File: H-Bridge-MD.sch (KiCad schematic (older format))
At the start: 67 parts, among them IC1 SI8650AB-B-IS1, IC2 A3921KLPTR-T, IC3 SI8650AB-B-IS1, IC4 A3921KLPTR-T, J1 Conn_01x02, J2 Conn_01x03, J3 Conn_01x05, J4 Conn_01x02, J5 Bus_mechaken_PCIexpress_x16_1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, Q1 NVMFD5C446NT1G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

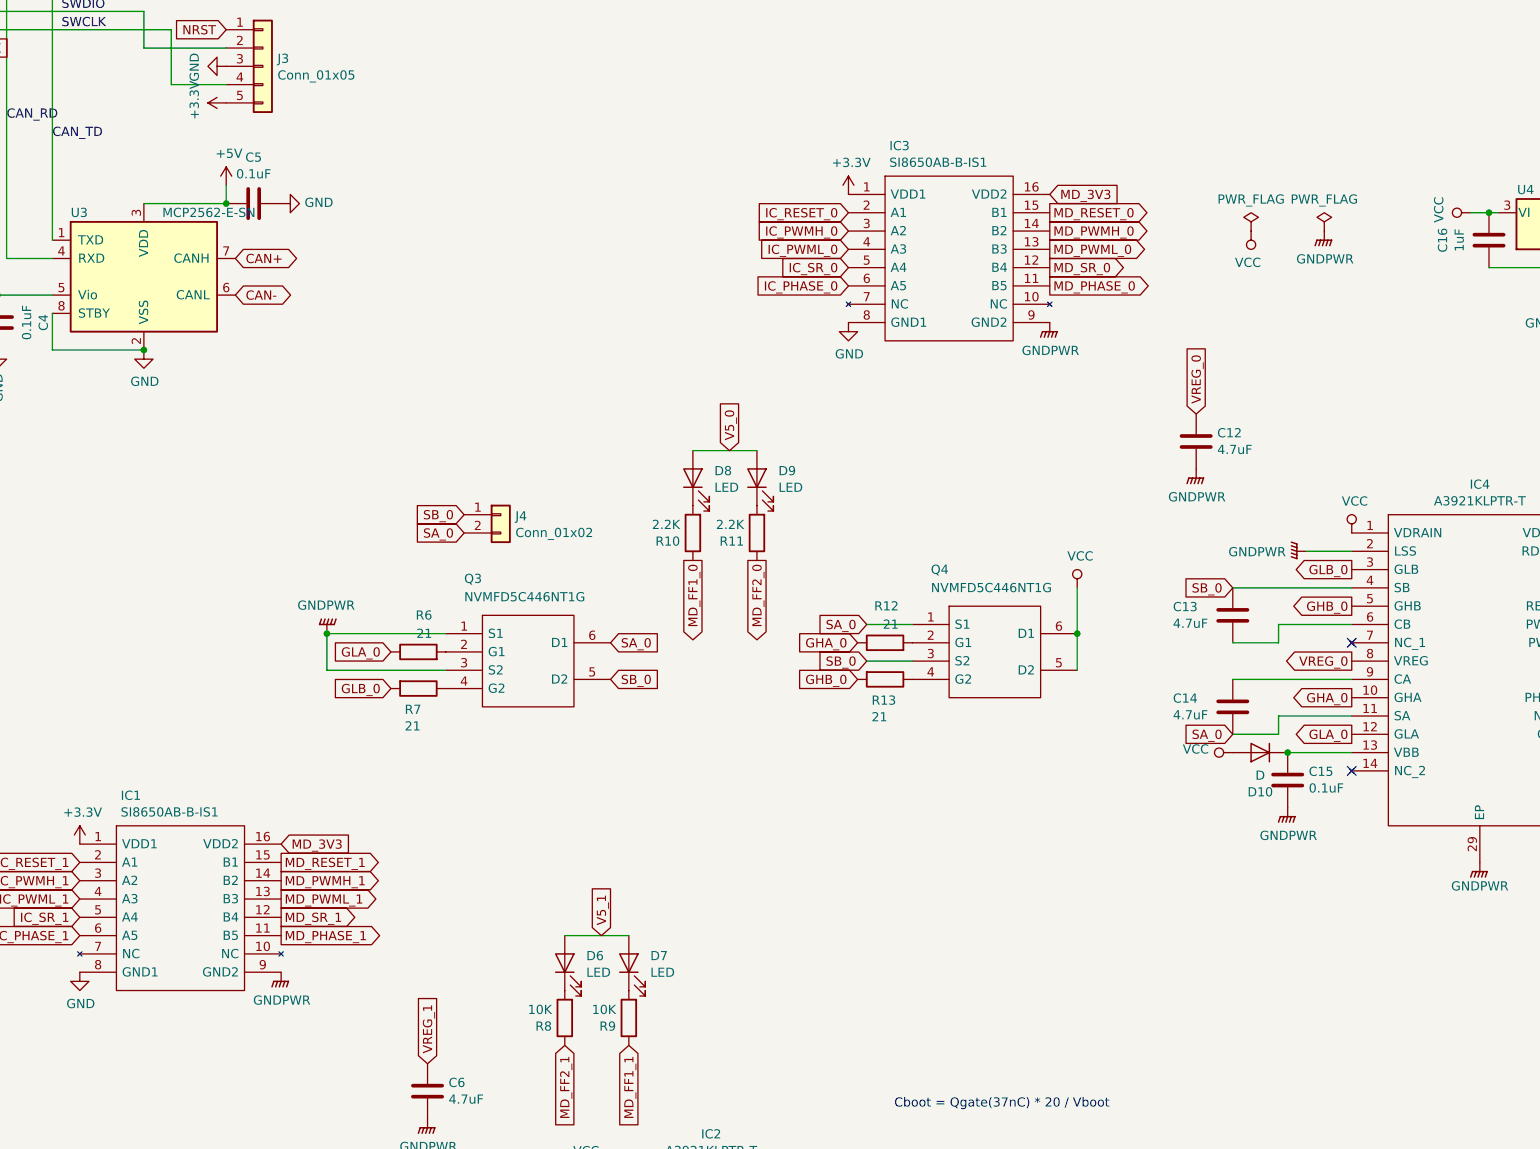
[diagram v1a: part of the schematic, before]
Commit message: change
書き込み用のピンをコンスルー対応に変更
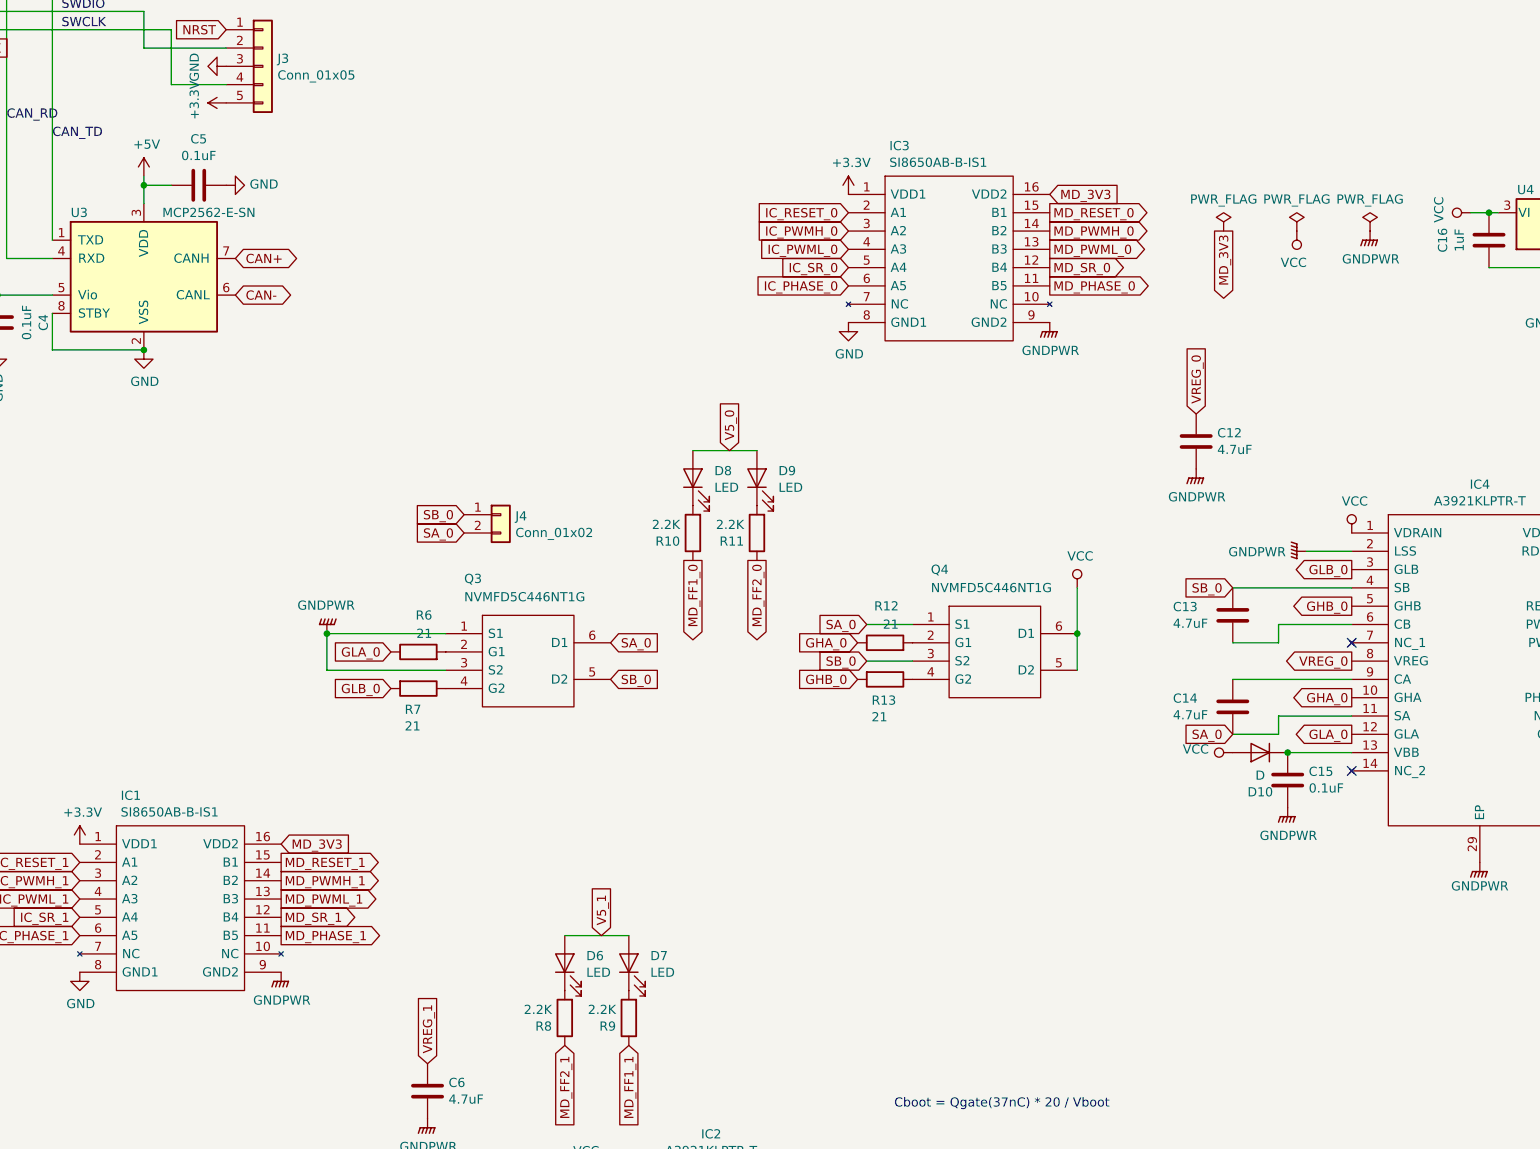
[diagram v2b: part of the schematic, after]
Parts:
- R8, R9: value 10K -> 2.2K
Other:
- moved on the sheet: C5
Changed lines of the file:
@@
-	1    0    0    -1
-$EndComp
-$Comp
-L power:PWR_FLAG #FLG04
-U 1 1 5DC02409
-P 11350 4100
-F 0 "#FLG04" H 11350 4175 50  0001 C CNN
-F 1 "PWR_FLAG" H 11350 4273 50  0000 C CNN
-F 2 "" H 11350 4100 50  0001 C CNN
-F 3 "~" H 11350 4100 50  0001 C CNN
-	1    11350 4100
-	1    0    0    -1
-$EndComp
-$Comp
-L power:PWR_FLAG #FLG05
-U 1 1 5DC02403
-P 11750 4100
-F 0 "#FLG05" H 11750 4175 50  0001 C CNN
-F 1 "PWR_FLAG" H 11750 4273 50  0000 C CNN
-F 2 "" H 11750 4100 50  0001 C CNN
-F 3 "~" H 11750 4100 50  0001 C CNN
-	1    11750 4100
 	1    0    0    -1
 $EndComp
@@
 L power:+5V #PWR022
 U 1 1 5D602945
-P 5750 3850
-F 0 "#PWR022" H 5750 3700 50  0001 C CNN
-F 1 "+5V" H 5765 4023 50  0000 C CNN
-F 2 "" H 5750 3850 50  0001 C CNN
-F 3 "" H 5750 3850 50  0001 C CNN
-	1    5750 3850
-	1    0    0    -1
-$EndComp
-Wire Wire Line
-	5750 3850 5750 3950
-Wire Wire Line
-	5750 3950 5300 3950
-$Comp
-L Device:C C5
-U 1 1 5D5F66CE
-P 5900 3950
-F 0 "C5" V 5648 3950 50  0000 C CNN
-F 1 "0.1uF" V 5739 3950 50  0000 C CNN
-F 2 "Capacitor_SMD:C_0805_2012Metric" H 5938 3800 50  0001 C CNN
-F 3 "~" H 5900 3950 50  0001 C CNN
-	1    5900 3950
-	0    1    1    0
-$EndComp
-$Comp
-L power:GND #PWR023
-U 1 1 5D5F66D4
-P 6050 3950
-F 0 "#PWR023" H 6050 3700 50  0001 C CNN
-F 1 "GND" V 6055 3822 50  0000 R CNN
-F 2 "" H 6050 3950 50  0001 C CNN
-F 3 "" H 6050 3950 50  0001 C CNN
-	1    6050 3950
-	0    -1   -1   0
-$EndComp
-Connection ~ 5750 3950
+P 5300 3800
+F 0 "#PWR022" H 5300 3650 50  0001 C CNN
+F 1 "+5V" H 5315 3973 50  0000 C CNN
+F 2 "" H 5300 3800 50  0001 C CNN
+F 3 "" H 5300 3800 50  0001 C CNN
+	1    5300 3800
+	1    0    0    -1
+$EndComp
 $Comp
 L Device:C C4
@@
 Wire Wire Line
 	9100 10800 9350 10800
-$Comp
-L power:VCC #PWR048
-U 1 1 5DC023F7
-P 11350 4100
-F 0 "#PWR048" H 11350 3950 50  0001 C CNN
-F 1 "VCC" H 11367 4273 50  0000 C CNN
-F 2 "" H 11350 4100 50  0001 C CNN
-F 3 "" H 11350 4100 50  0001 C CNN
-	1    11350 4100
-	-1   0    0    1
-$EndComp
-$Comp
-L power:GNDPWR #PWR051
-U 1 1 5DC023FD
-P 11750 4100
-F 0 "#PWR051" H 11750 3900 50  0001 C CNN
-F 1 "GNDPWR" H 11754 3946 50  0000 C CNN
-F 2 "" H 11750 4050 50  0001 C CNN
-F 3 "" H 11750 4050 50  0001 C CNN
-	1    11750 4100
-	1    0    0    -1
-$EndComp
 Connection ~ 9850 10400
 Wire Wire Line
@@
 Text GLabel 10250 4100 2    50   Output ~ 0
 MD_PWMH_0
-Text GLabel 10250 4400 2    50   Output ~ 0
-MD_PHASE_0
 Text GLabel 4200 2300 2    50   Output ~ 0
 IC_PWMH_1
-Text GLabel 10250 4000 2    50   Output ~ 0
-MD_RESET_0
 Text GLabel 3200 2400 0    50   Output ~ 0
 IC_RESET_1
@@
 	1    0    0    -1
 $EndComp
-Text GLabel 11050 5100 1    50   Input ~ 0
-VREG_0
 $Comp
 L power:GNDPWR #PWR043
@@
 P 7600 8400
 F 0 "R8" H 7670 8446 50  0000 L CNN
-F 1 "10K" H 7670 8355 50  0000 L CNN
+F 1 "2.2K" H 7670 8355 50  0000 L CNN
 F 2 "Resistor_SMD:R_0603_1608Metric" V 7530 8400 50  0001 C CNN
 F 3 "~" H 7600 8400 50  0001 C CNN
@@
 P 7950 8400
 F 0 "R9" H 8020 8446 50  0000 L CNN
-F 1 "10K" H 8020 8355 50  0000 L CNN
+F 1 "2.2K" H 8020 8355 50  0000 L CNN
 F 2 "Resistor_SMD:R_0603_1608Metric" V 7880 8400 50  0001 C CNN
 F 3 "~" H 7950 8400 50  0001 C CNN
@@
 Wire Wire Line
 	7600 7950 7950 7950
+Text GLabel 10250 4000 2    50   Output ~ 0
+MD_RESET_0
+Text GLabel 10250 4400 2    50   Output ~ 0
+MD_PHASE_0
+$Comp
+L power:PWR_FLAG #FLG04
+U 1 1 5DC02409
+P 11600 4100
+F 0 "#FLG04" H 11600 4175 50  0001 C CNN
+F 1 "PWR_FLAG" H 11600 4273 50  0000 C CNN
+F 2 "" H 11600 4100 50  0001 C CNN
+F 3 "~" H 11600 4100 50  0001 C CNN
+	1    11600 4100
+	1    0    0    -1
+$EndComp
+$Comp
+L power:PWR_FLAG #FLG05
+U 1 1 5DC02403
+P 12000 4100
+F 0 "#FLG05" H 12000 4175 50  0001 C CNN
+F 1 "PWR_FLAG" H 12000 4273 50  0000 C CNN
+F 2 "" H 12000 4100 50  0001 C CNN
+F 3 "~" H 12000 4100 50  0001 C CNN
+	1    12000 4100
+	1    0    0    -1
+$EndComp
+$Comp
+L power:VCC #PWR048
+U 1 1 5DC023F7
+P 11600 4100
+F 0 "#PWR048" H 11600 3950 50  0001 C CNN
+F 1 "VCC" H 11617 4273 50  0000 C CNN
+F 2 "" H 11600 4100 50  0001 C CNN
+F 3 "" H 11600 4100 50  0001 C CNN
+	1    11600 4100
+	-1   0    0    1
+$EndComp
+$Comp
+L power:GNDPWR #PWR051
+U 1 1 5DC023FD
+P 12000 4100
+F 0 "#PWR051" H 12000 3900 50  0001 C CNN
+F 1 "GNDPWR" H 12004 3946 50  0000 C CNN
+F 2 "" H 12000 4050 50  0001 C CNN
+F 3 "" H 12000 4050 50  0001 C CNN
+	1    12000 4100
+	1    0    0    -1
+$EndComp
+$Comp
+L power:PWR_FLAG #FLG0101
+U 1 1 5E1278AA
+P 11200 4100
+F 0 "#FLG0101" H 11200 4175 50  0001 C CNN
+F 1 "PWR_FLAG" H 11200 4273 50  0000 C CNN
+F 2 "" H 11200 4100 50  0001 C CNN
+F 3 "~" H 11200 4100 50  0001 C CNN
+	1    11200 4100
+	1    0    0    -1
+$EndComp
+Text GLabel 11200 4100 3    50   Output ~ 0
+MD_3V3
+Text GLabel 11050 5100 1    50   Input ~ 0
+VREG_0
+$Comp
+L power:GND #PWR023
+U 1 1 5D5F66D4
+P 5750 3850
+F 0 "#PWR023" H 5750 3600 50  0001 C CNN
+F 1 "GND" V 5755 3722 50  0000 R CNN
+F 2 "" H 5750 3850 50  0001 C CNN
+F 3 "" H 5750 3850 50  0001 C CNN
+	1    5750 3850
+	0    -1   -1   0
+$EndComp
+$Comp
+L Device:C C5
+U 1 1 5D5F66CE
+P 5600 3850
+F 0 "C5" V 5348 3850 50  0000 C CNN
+F 1 "0.1uF" V 5439 3850 50  0000 C CNN
+F 2 "Capacitor_SMD:C_0805_2012Metric" H 5638 3700 50  0001 C CNN
+F 3 "~" H 5600 3850 50  0001 C CNN
+	1    5600 3850
+	0    1    1    0
+$EndComp
+Wire Wire Line
+	5300 3800 5300 3850
+Wire Wire Line
+	5300 3850 5450 3850
+Connection ~ 5300 3850
+Wire Wire Line
+	5300 3850 5300 3950
 $EndSCHEMATC

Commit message: change
抵抗アレイを1206に変更
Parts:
- RN1: footprint Resistor_SMD:R_Array_Concave_4x0603 -> Resistor_SMD:R_Array_Convex_4x1206
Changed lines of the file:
@@
 F 0 "RN1" V 900 2900 50  0000 C CNN
 F 1 "R_Pack04" V 1400 2900 50  0000 C CNN
-F 2 "Resistor_SMD:R_Array_Concave_4x0603" V 1475 2900 50  0001 C CNN
+F 2 "Resistor_SMD:R_Array_Convex_4x1206" V 1475 2900 50  0001 C CNN
 F 3 "~" H 1200 2900 50  0001 C CNN
 	1    1200 2900

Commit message: change
ダイオードのフットプリントをハーフホール向けに変更
その他の微修正（主に配線）
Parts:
- D1, D2, D3, D4, D6, D7, D8, D9: footprint LED_SMD:LED_0603_1608Metric -> LED_SMD:LED_0603_1608Metric_Castellated
- D10: footprint Diode_SMD:D_0603_1608Metric -> LED_SMD:LED_0603_1608Metric_Castellated
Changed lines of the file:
@@
 F 0 "D10" H 11400 7166 50  0000 C CNN
 F 1 "D" H 11400 7075 50  0000 C CNN
-F 2 "Diode_SMD:D_0603_1608Metric" H 11400 6950 50  0001 C CNN
+F 2 "LED_SMD:LED_0603_1608Metric_Castellated" H 11400 6950 50  0001 C CNN
 F 3 "~" H 11400 6950 50  0001 C CNN
 	1    11400 6950
@@
 F 0 "D3" V 1339 3212 50  0000 C CNN
 F 1 "LED" V 1248 3212 50  0000 C CNN
-F 2 "LED_SMD:LED_0603_1608Metric" H 1300 3400 50  0001 C CNN
+F 2 "LED_SMD:LED_0603_1608Metric_Castellated" H 1300 3400 50  0001 C CNN
 F 3 "~" H 1300 3400 50  0001 C CNN
 	1    1300 3400
@@
 F 0 "D2" V 1039 3212 50  0000 C CNN
 F 1 "LED" V 948 3212 50  0000 C CNN
-F 2 "LED_SMD:LED_0603_1608Metric" H 1000 3400 50  0001 C CNN
+F 2 "LED_SMD:LED_0603_1608Metric_Castellated" H 1000 3400 50  0001 C CNN
 F 3 "~" H 1000 3400 50  0001 C CNN
 	1    1000 3400
@@
 F 0 "D1" V 739 3550 50  0000 C CNN
 F 1 "LED" V 648 3550 50  0000 C CNN
-F 2 "LED_SMD:LED_0603_1608Metric" H 700 3400 50  0001 C CNN
+F 2 "LED_SMD:LED_0603_1608Metric_Castellated" H 700 3400 50  0001 C CNN
 F 3 "~" H 700 3400 50  0001 C CNN
 	1    700  3400
@@
 F 0 "D4" V 1639 3212 50  0000 C CNN
 F 1 "LED" V 1548 3212 50  0000 C CNN
-F 2 "LED_SMD:LED_0603_1608Metric" H 1600 3400 50  0001 C CNN
+F 2 "LED_SMD:LED_0603_1608Metric_Castellated" H 1600 3400 50  0001 C CNN
 F 3 "~" H 1600 3400 50  0001 C CNN
 	1    1600 3400
@@
 F 0 "D6" V 7639 7983 50  0000 R CNN
 F 1 "LED" V 7548 7983 50  0000 R CNN
-F 2 "LED_SMD:LED_0603_1608Metric" H 7600 8100 50  0001 C CNN
+F 2 "LED_SMD:LED_0603_1608Metric_Castellated" H 7600 8100 50  0001 C CNN
 F 3 "~" H 7600 8100 50  0001 C CNN
 	1    7600 8100
@@
 F 0 "D7" V 7989 7983 50  0000 R CNN
 F 1 "LED" V 7898 7983 50  0000 R CNN
-F 2 "LED_SMD:LED_0603_1608Metric" H 7950 8100 50  0001 C CNN
+F 2 "LED_SMD:LED_0603_1608Metric_Castellated" H 7950 8100 50  0001 C CNN
 F 3 "~" H 7950 8100 50  0001 C CNN
 	1    7950 8100
@@
 F 0 "D9" V 8689 5333 50  0000 R CNN
 F 1 "LED" V 8598 5333 50  0000 R CNN
-F 2 "LED_SMD:LED_0603_1608Metric" H 8650 5450 50  0001 C CNN
+F 2 "LED_SMD:LED_0603_1608Metric_Castellated" H 8650 5450 50  0001 C CNN
 F 3 "~" H 8650 5450 50  0001 C CNN
 	1    8650 5450
@@
 F 0 "D8" V 8339 5333 50  0000 R CNN
 F 1 "LED" V 8248 5333 50  0000 R CNN
-F 2 "LED_SMD:LED_0603_1608Metric" H 8300 5450 50  0001 C CNN
+F 2 "LED_SMD:LED_0603_1608Metric_Castellated" H 8300 5450 50  0001 C CNN
 F 3 "~" H 8300 5450 50  0001 C CNN
 	1    8300 5450
